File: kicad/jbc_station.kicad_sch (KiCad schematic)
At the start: 120 parts, among them J1 PWR, J2 Conn_01x02, J3 Barcode, J4 Front panel, J5 Conn_01x03, J6 Conn_01x05, J7 Conn_01x04, J8 Conn_01x03, Q1 BSS138, Q2 BSS138, Q3 BSS138, U1 L78L05_SOT89, U10 CH9141K, U2 LP2985-3.3, U3 ICL7660, U4 HT7463, U5 HT7463, U6 XC6206PxxxMR, U7 M24C64, U8 INA3221, U9 STM32F401CCUx, Y1 Crystal, Y2 Crystal

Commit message: Route finish
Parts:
- removed L5: 1u, Inductor_SMD:L_1206_3216Metric_Pad1.22x1.90mm_HandSolder, symbol Device:L
- removed NT2, NT3: NetTie_2, NetTie:NetTie-2_SMD_Pad2.0mm, symbol Device:NetTie_2
- added C30, C99: 2.2u, Capacitor_SMD:C_0805_2012Metric, symbol Device:C
- added U17: XC6206PxxxMR, Package_TO_SOT_SMD:SOT-23-3, symbol Regulator_Linear:XC6206PxxxMR
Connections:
- net +3V3 is gone; now on net +3.3V: J6.1 (Pin_1)
- net +5V: no longer R25.2
- net +5VL: now also R25.2
- net +5VSB: now also C99.1, U17.3 (VI)
- net GND: now also C10.2, C9.1, H3.1, H5.1, NT1.2, U1.2 (GND), C30.2, C99.2, U17.1 (GND)
- net int-out1/I_{SEN+}: now also R13.1; no longer R9.1
- net int-out1/I_{SEN-}: now also R15.1; no longer R10.1
- net int-out2/I_{SEN+}: now also R16.1; no longer R13.1
- net int-out2/I_{SEN-}: now also R17.1; no longer R15.1
- net int-out3/I_{SEN+}: now also R9.1; no longer R16.1
- net int-out3/I_{SEN-}: now also R10.1; no longer R17.1
- net at C38.2, C39.2, J7.4 (Pin_4)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: now also C30.1, U17.2 (VO)

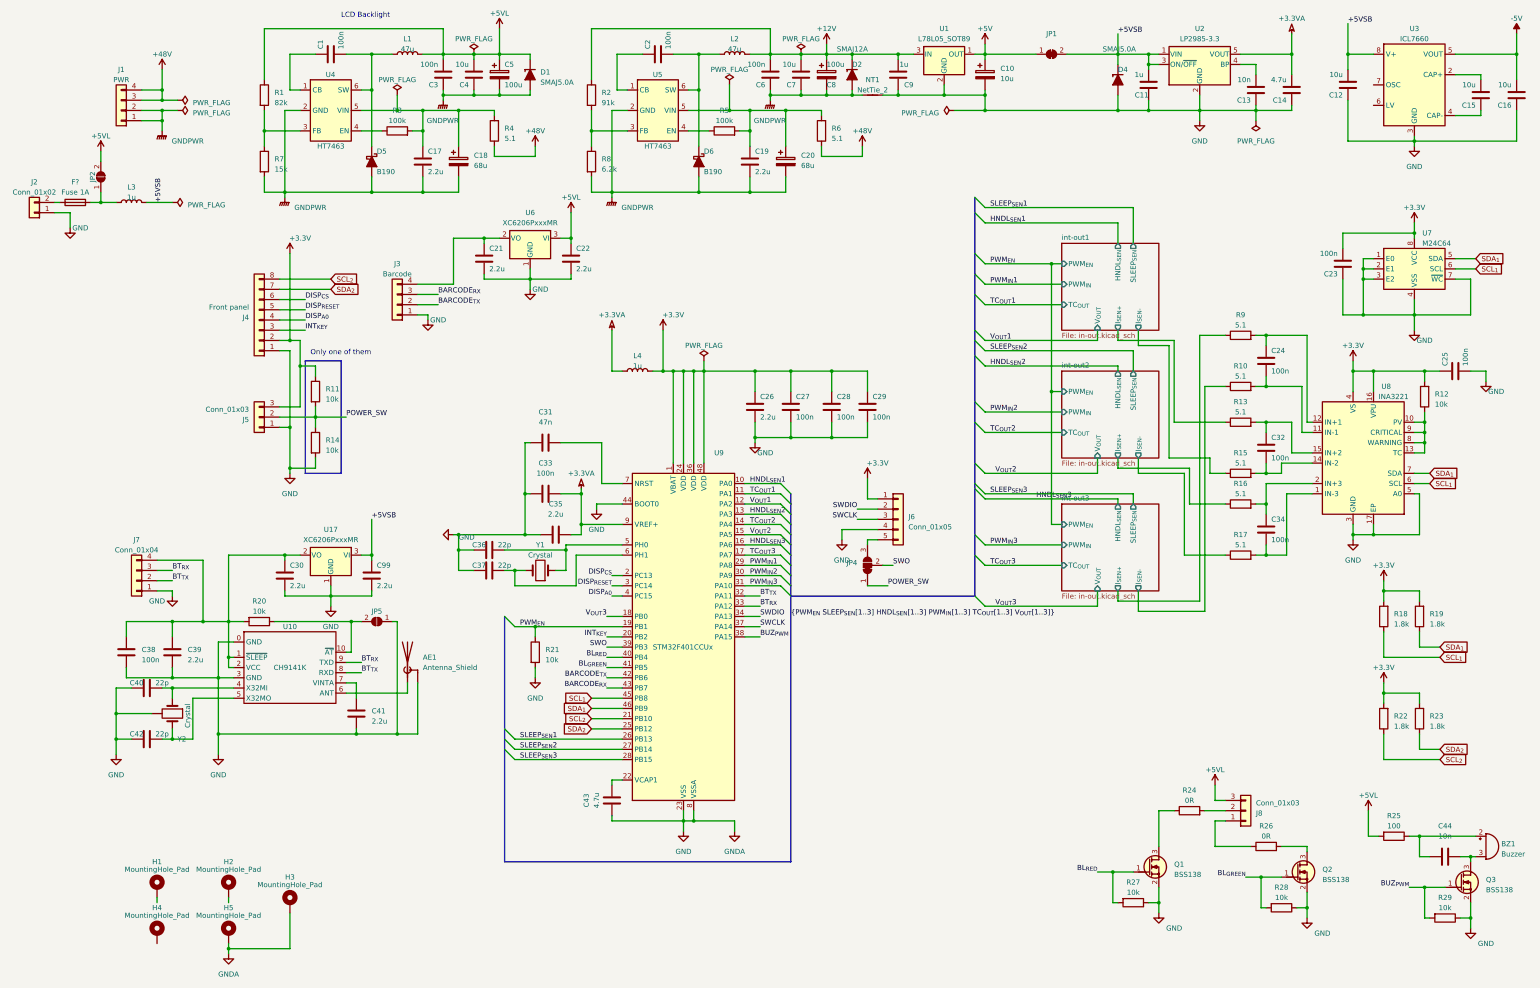
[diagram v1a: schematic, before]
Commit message: Add more filtering caps for ADC
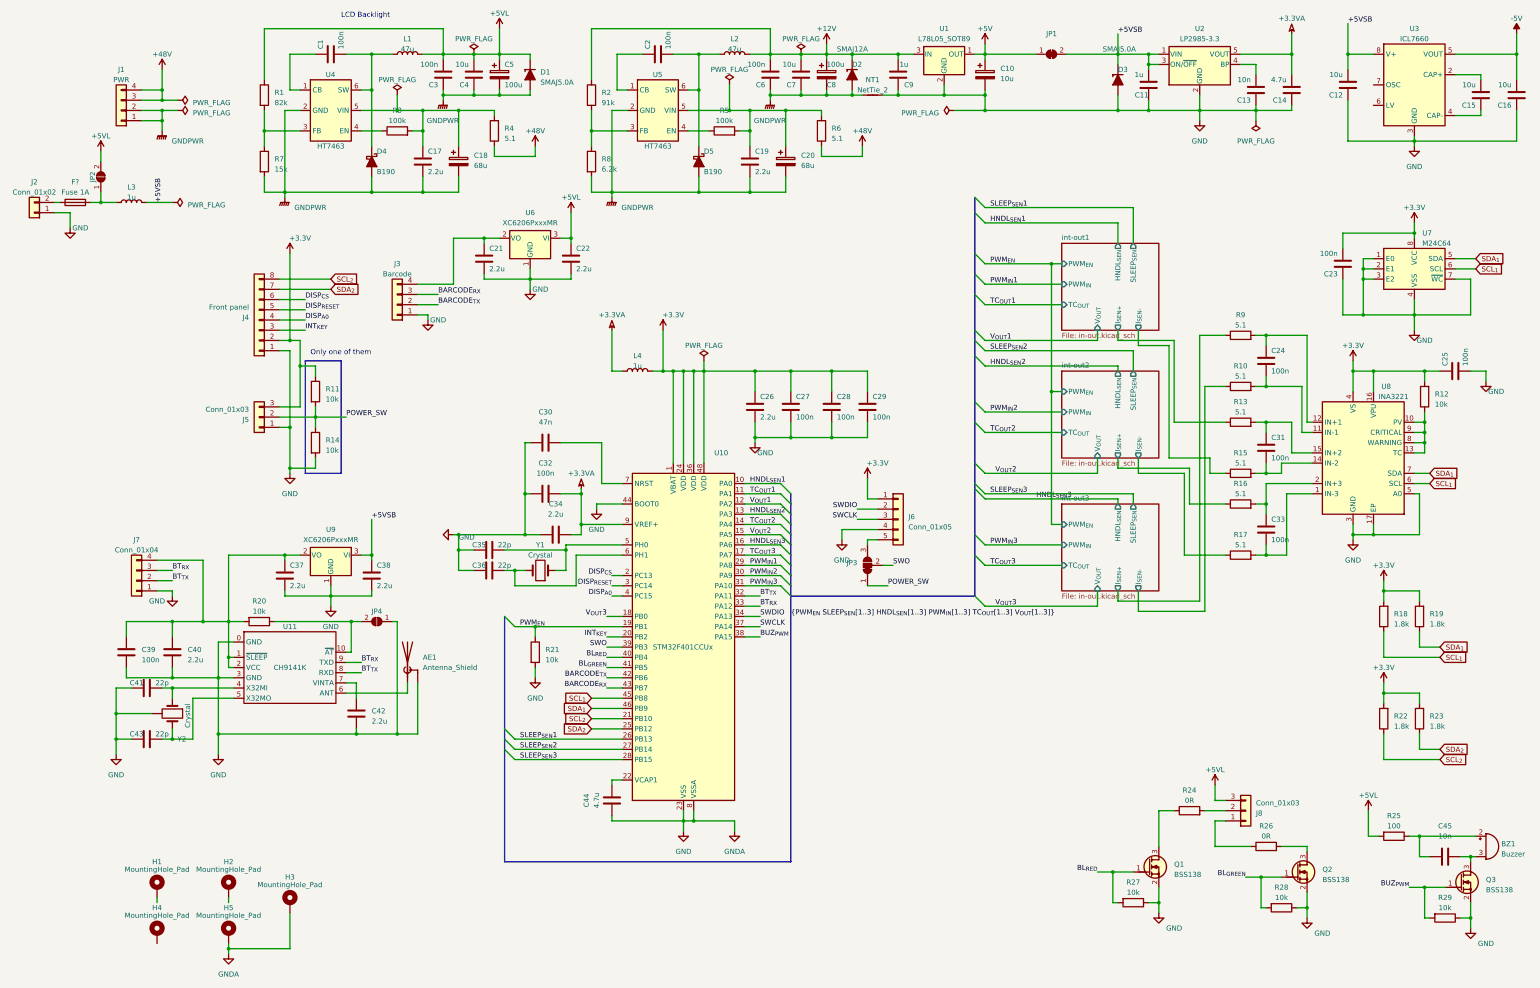
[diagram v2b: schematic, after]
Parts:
- renumbered C31 to C30, C32 to C31, C33 to C32, C34 to C33, C35 to C34, C36 to C35, C37 to C36, C30 to C37, C99 to C38, C38 to C39, C39 to C40, C40 to C41, C41 to C42, C42 to C43, C43 to C44, C44 to C45, D4 to D3, D5 to D4, D6 to D5, JP4 to JP3, JP5 to JP4, U9 to U10, U10 to U11, U17 to U9

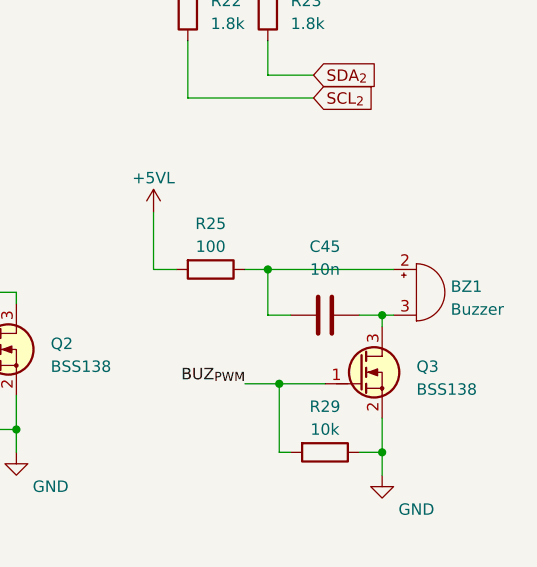
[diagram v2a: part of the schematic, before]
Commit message: Various minor fixes based on production samples
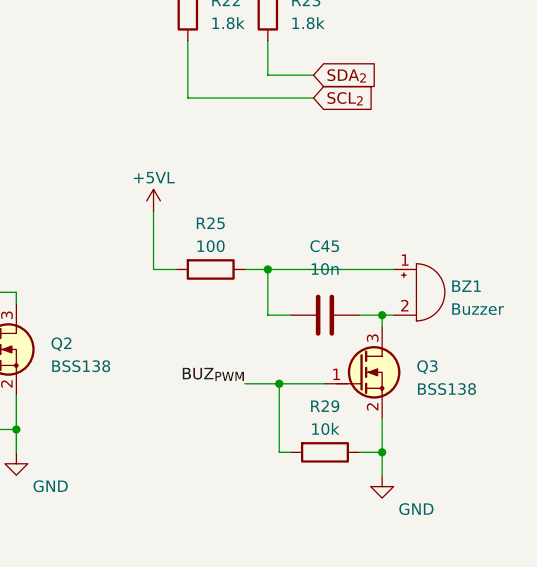
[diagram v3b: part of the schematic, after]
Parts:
- C12, C14, C15, C16, C17, C19, C4, C7: footprint Capacitor_SMD:C_0805_2012Metric -> Capacitor_SMD:C_1206_3216Metric_Pad1.33x1.80mm_HandSolder
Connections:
- net at C45.1, R25.1: now also BZ1.1 (-); no longer BZ1.2 (+)
- net at C45.2, Q3.3 (D): now also BZ1.2 (+); no longer BZ1.3 (-)
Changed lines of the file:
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@@
       (effects (font (size 1.27 1.27)) (justify left))
     )
-    (property "Footprint" "Capacitor_SMD:C_0805_2012Metric" (at 217.4748 30.48 0)
+    (property "Footprint" "Capacitor_SMD:C_1206_3216Metric_Pad1.33x1.80mm_HandSolder" (at 217.4748 30.48 0)
       (effects (font (size 1.27 1.27)) hide)
     )
@@
       (effects (font (size 1.27 1.27)) hide)
     )
+    (pin "1")
     (pin "2")
-    (pin "3")
     (instances
       (project "jbc_station"
@@
       (effects (font (size 1.27 1.27)) (justify left))
     )
-    (property "Footprint" "Capacitor_SMD:C_0805_2012Metric" (at 395.2748 35.56 0)
+    (property "Footprint" "Capacitor_SMD:C_1206_3216Metric_Pad1.33x1.80mm_HandSolder" (at 395.2748 35.56 0)
       (effects (font (size 1.27 1.27)) hide)
     )
@@
       (effects (font (size 1.27 1.27)) (justify left))
     )
-    (property "Footprint" "Capacitor_SMD:C_0805_2012Metric" (at 125.4252 59.69 0)
+    (property "Footprint" "Capacitor_SMD:C_1206_3216Metric_Pad1.33x1.80mm_HandSolder" (at 125.4252 59.69 0)
       (effects (font (size 1.27 1.27)) hide)
     )
@@
       (effects (font (size 1.27 1.27)) (justify left))
     )
-    (property "Footprint" "Capacitor_SMD:C_0805_2012Metric" (at 386.3848 35.56 0)
+    (property "Footprint" "Capacitor_SMD:C_1206_3216Metric_Pad1.33x1.80mm_HandSolder" (at 386.3848 35.56 0)
       (effects (font (size 1.27 1.27)) hide)
     )
@@
       (effects (font (size 1.27 1.27)) (justify left))
     )
-    (property "Footprint" "Capacitor_SMD:C_0805_2012Metric" (at 206.7052 59.69 0)
+    (property "Footprint" "Capacitor_SMD:C_1206_3216Metric_Pad1.33x1.80mm_HandSolder" (at 206.7052 59.69 0)
       (effects (font (size 1.27 1.27)) hide)
     )
@@
       (effects (font (size 1.27 1.27)) (justify left))
     )
-    (property "Footprint" "Capacitor_SMD:C_0805_2012Metric" (at 136.1948 30.48 0)
+    (property "Footprint" "Capacitor_SMD:C_1206_3216Metric_Pad1.33x1.80mm_HandSolder" (at 136.1948 30.48 0)
       (effects (font (size 1.27 1.27)) hide)
     )
@@
       (effects (font (size 1.27 1.27)) (justify left))
     )
-    (property "Footprint" "Capacitor_SMD:C_0805_2012Metric" (at 353.3648 33.02 0)
+    (property "Footprint" "Capacitor_SMD:C_1206_3216Metric_Pad1.33x1.80mm_HandSolder" (at 353.3648 33.02 0)
       (effects (font (size 1.27 1.27)) hide)
     )
@@
       (effects (font (size 1.27 1.27)) (justify left))
     )
-    (property "Footprint" "Capacitor_SMD:C_0805_2012Metric" (at 339.3948 34.29 0)
+    (property "Footprint" "Capacitor_SMD:C_1206_3216Metric_Pad1.33x1.80mm_HandSolder" (at 339.3948 34.29 0)
       (effects (font (size 1.27 1.27)) hide)
     )

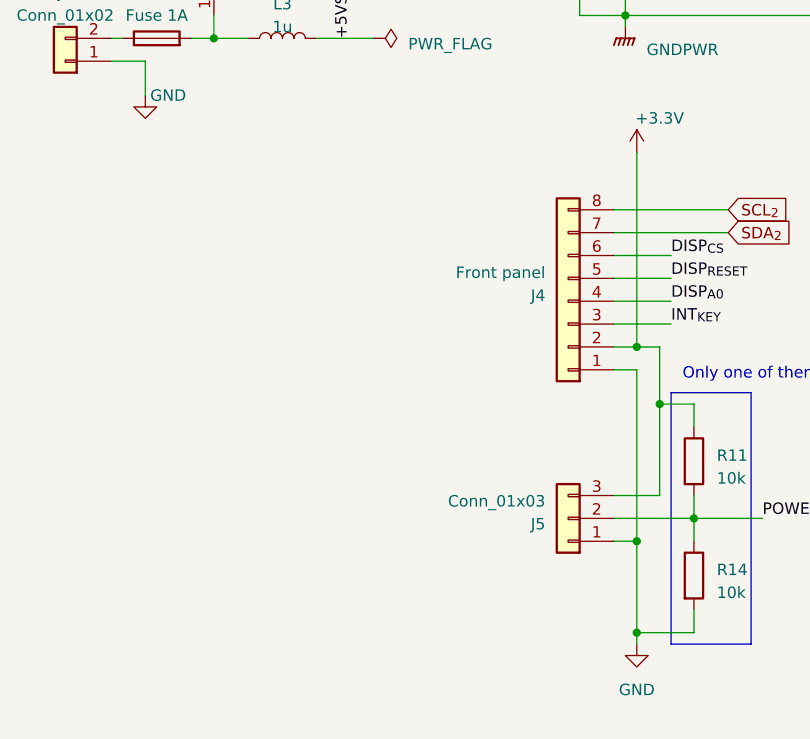
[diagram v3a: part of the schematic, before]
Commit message: Add front panel schematic based on 74HC164
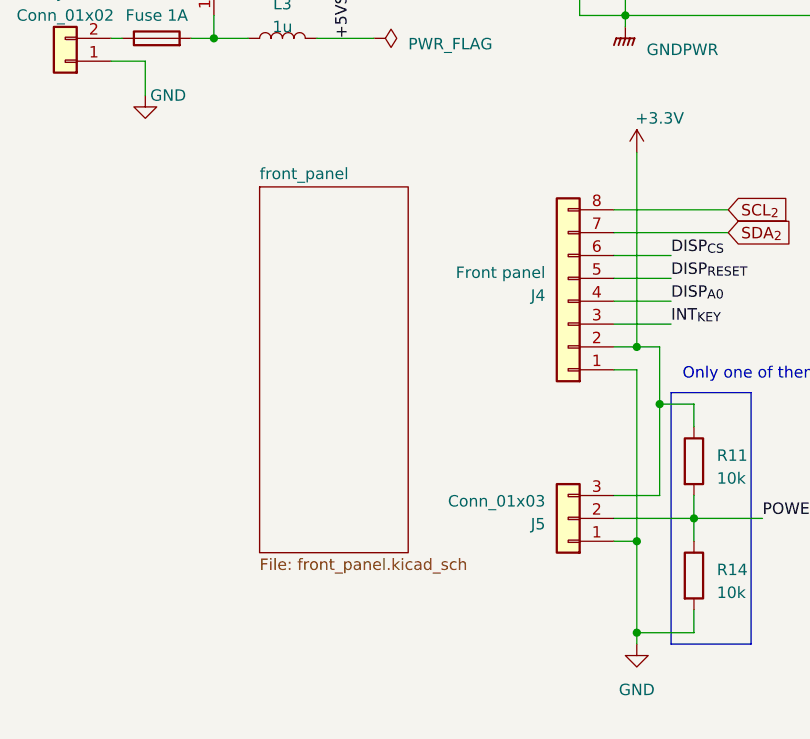
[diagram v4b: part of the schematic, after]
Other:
- added sheet front_panel (front_panel.kicad_sch)
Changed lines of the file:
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@@
+    )
+  )
+  (sheet (at 49.53 82.55) (size 16.51 40.64) (fields_autoplaced)
+    (stroke (width 0.1524) (type solid))
+    (fill (color 0 0 0 0.0000))
+    (property "Sheetname" "front_panel" (at 49.53 81.8384 0)
+      (effects (font (size 1.27 1.27)) (justify left bottom))
+    )
+    (property "Sheetfile" "front_panel.kicad_sch" (at 49.53 123.7746 0)
+      (effects (font (size 1.27 1.27)) (justify left top))
+    )
+    (instances
+      (project "jbc_station"
+        (path "/d4547348-927f-40d5-95cc-3315216c85d1" (page "5"))
+      )
     )
   )
